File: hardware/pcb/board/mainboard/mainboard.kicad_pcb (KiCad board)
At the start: 6 copper layers, 76.4 x 55 mm, 137 parts, among them J1 Conn_Coaxial, J10 USB_C_Receptacle, J11 2908-05WB-MG, J2 USB_C_Receptacle_USB2.0_16P, J3 Conn_02x35_Odd_Even_MountingP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, J4 Conn_02x40_Odd_Even_MountingP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, J5 Conn_02x40_Odd_Even_MountingP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, J7 Conn_01x30, J8 Conn_01x30, J9 Conn_01x30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

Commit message: USB PD power
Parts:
- moved R18 33.9 mm to (169.0, 147.7), turned to 0 degrees
- moved R19 32.3 mm to (169.0, 146.1), turned to 0 degrees
- moved U14 24.1 mm to (168.2, 151.9), turned to 90 degrees
- moved C27 20.8 mm to (169.0, 149.3), turned to 0 degrees
- moved C26 18.5 mm to (162.1, 146.1)
- moved R22 16.1 mm to (149.8, 134.3)
- moved C33 16.1 mm to (153.0, 134.3)
- moved C34 16.1 mm to (152.9, 135.9)
- moved U12 10.2 mm to (158.2, 138.0), turned to 180 degrees
- moved R24 9.94 mm to (166.2, 133.6)
- moved R26 9.94 mm to (166.2, 135.2)
- moved C28 7.85 mm to (162.0, 140.6), turned to 0 degrees
- moved R23 6.24 mm to (159.0, 146.1), turned to 0 degrees
- moved C32 4.93 mm to (164.3, 138.3), turned to -90 degrees
- moved Q2 4.80 mm to (161.4, 143.3), turned to 0 degrees
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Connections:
- J2 pad GND: (no net) -> GND
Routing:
- net H_UART_RXD_1: track 0.00 -> 25.4 mm
- net H_UART_TXD_1: track 0.00 -> 25.0 mm
- net USB1_D-: track 0.00 -> 12.4 mm, vias 0 -> 3
- net USB1_D+: track 0.00 -> 11.3 mm, vias 0 -> 2
- net +1V8: track 0.00 -> 8.29 mm, vias 0 -> 2
- net USB1_VBUS: track 0.00 -> 7.45 mm
- net Net-(J2-CC2): track 0.00 -> 6.18 mm, vias 0 -> 2
- net Net-(J2-CC1): track 0.00 -> 4.68 mm
- net VBUS: track 0.00 -> 2.81 mm
- net GND: track 0.00 -> 1.83 mm
- net USB_D-: track 0.00 -> 1.61 mm
- net USB_D+: track 0.00 -> 0.75 mm, vias 0 -> 1
- added copper zone on B.Cu, net GND
- added copper zone on F.Cu, net GND
- added copper zone on In1.Cu, net GND
- added copper zone on In4.Cu, net GND

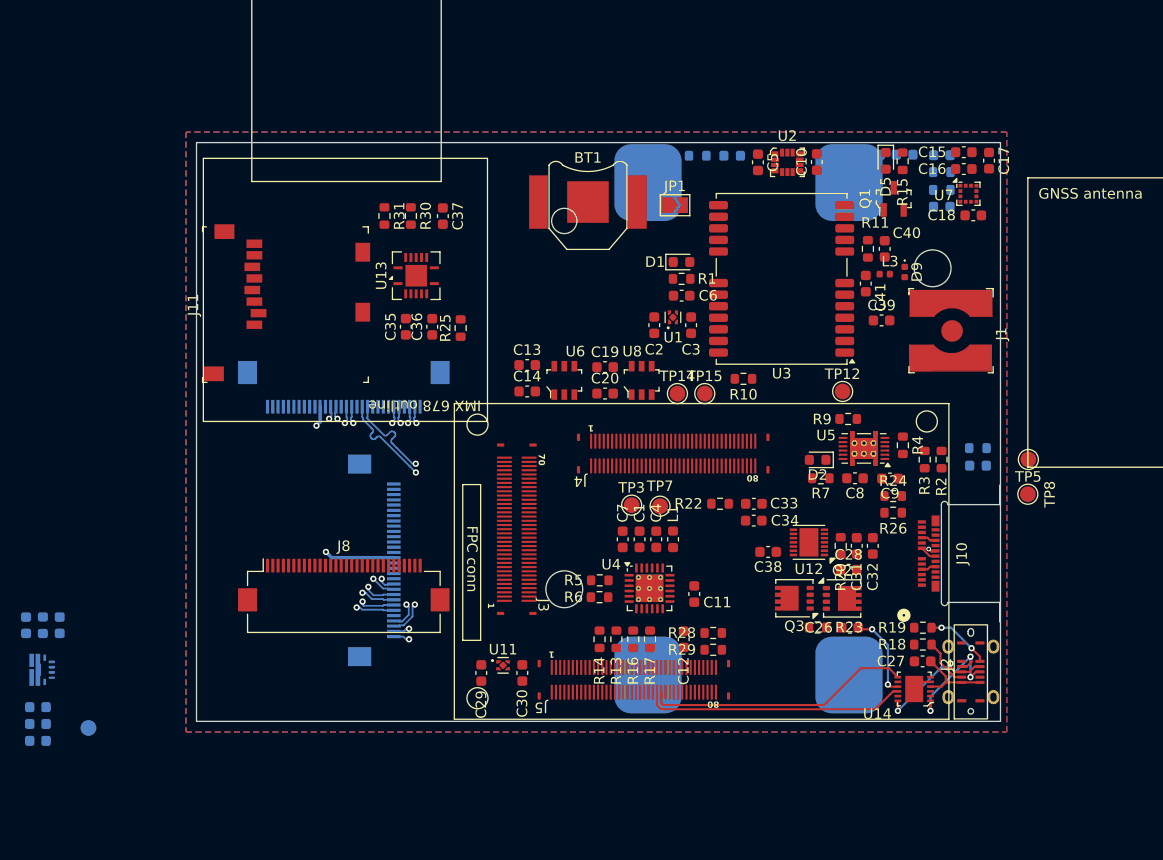
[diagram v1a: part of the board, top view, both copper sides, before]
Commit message: BQ25606 routing
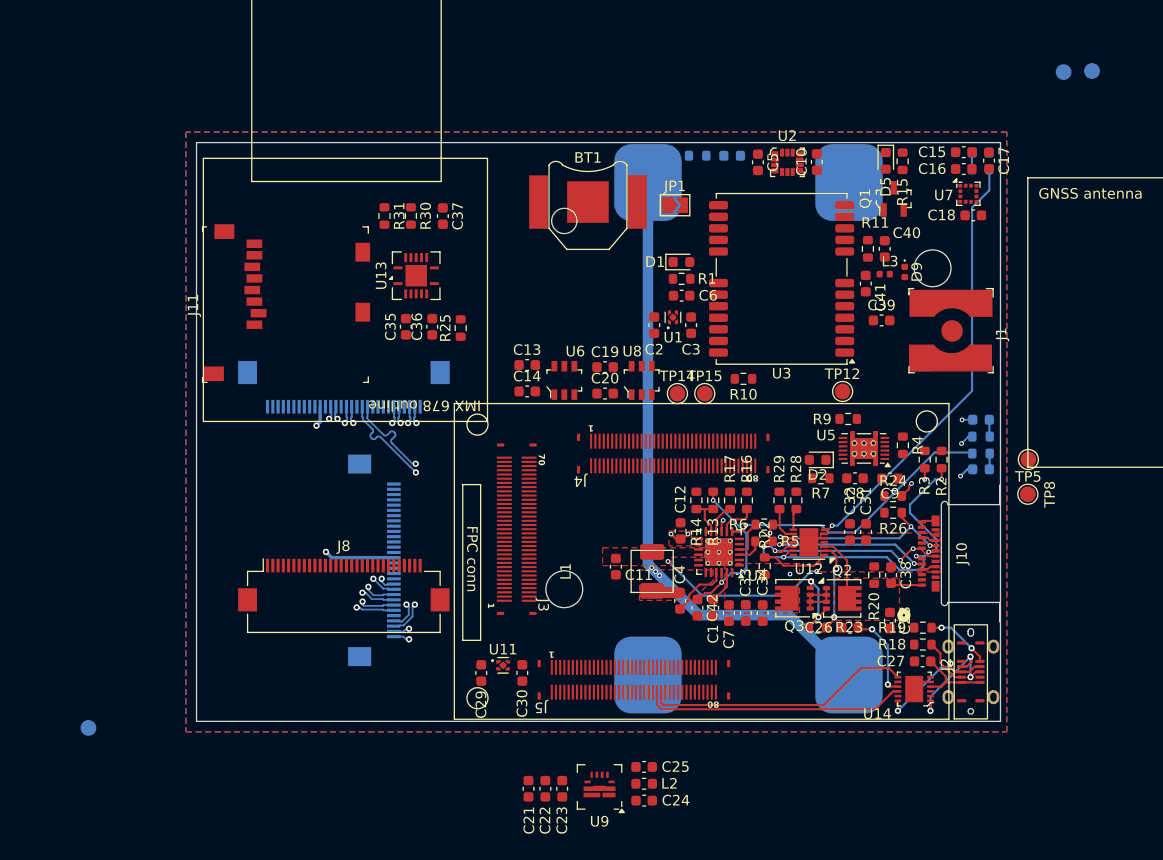
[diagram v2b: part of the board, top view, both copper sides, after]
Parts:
- removed D6: LED, LED_SMD:LED_0603_1608Metric
- removed R21: 100k, Resistor_SMD:R_0603_1608Metric
- added C42: 4.7 uF, Capacitor_SMD:C_0603_1608Metric, F.Cu at (147.6, 144.2)
- C21, C22, C23, C24, C25, L2, U9: moved to F.Cu
- L1: footprint Inductor_SMD:L_0603_1608Metric -> unsurv_offline_pcb_footprints:Inductor_Wuerth_74437321010
- TP3, TP7: moved to B.Cu
- moved C24 61.1 mm to (142.5, 162.5), turned to 180 degrees
- moved L2 59.1 mm to (142.5, 160.9), turned to 180 degrees
- moved TP7 58.3 mm to (185.1, 93.2)
- moved TP3 58.1 mm to (182.4, 93.3)
- moved C25 57.1 mm to (142.5, 159.3), turned to 180 degrees
- moved U9 54.4 mm to (138.3, 161.2), turned to 180 degrees
- moved C23 50.4 mm to (134.8, 161.4), turned to 90 degrees
- moved C22 48.6 mm to (133.2, 161.4), turned to 90 degrees
- moved C21 46.8 mm to (131.6, 161.4), turned to 90 degrees
- moved D4 30.8 mm to (174.6, 131.1)
- moved R12 30.2 mm to (174.6, 129.6)
- moved R32 23.7 mm to (174.6, 127.9)
- moved D8 20.6 mm to (174.6, 126.3), turned to 0 degrees
- moved R6 17.1 mm to (153.9, 136.3)
- moved R16 17.1 mm to (152.3, 134.0), turned to 90 degrees
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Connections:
- BT2 pad 2: B- -> GND
- J2 pad GND: GND -> (no net)
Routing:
- net B+: track 0.00 -> 61.7 mm, vias 0 -> 5
- net Net-(U12-LED): track 0.00 -> 41.2 mm, vias 0 -> 1
- net SYS: track 0.00 -> 35.3 mm, vias 0 -> 3
- net USB_D+: track 0.75 -> 33.6 mm, vias 1 -> 5
- net USB_D-: track 1.61 -> 30.3 mm, vias 0 -> 5
- net Net-(U4-PG): track 0.00 -> 26.7 mm, vias 0 -> 1
- net USB_CC1: track 0.00 -> 25.8 mm, vias 0 -> 3
- net USB_PD: track 0.00 -> 24.6 mm, vias 0 -> 2
- net USB_CC2: track 0.00 -> 19.0 mm, vias 0 -> 3
- net REGN: track 0.00 -> 15.4 mm, vias 0 -> 2
- net Net-(U12-PWR_EN): track 0.00 -> 8.51 mm, vias 0 -> 2
- net GND: track 1.83 -> 9.97 mm, vias 0 -> 2
- net Net-(Q2-G): track 0.00 -> 6.82 mm, vias 0 -> 2
- net Net-(U12-VOUT): track 0.00 -> 6.42 mm
- net Net-(Q2-D): track 0.00 -> 6.29 mm
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- added copper zone on F.Cu, net B+
- added copper zone on In3.Cu, net B+
- added copper zone on F.Cu, net Net-(C4-Pad2)
- added copper zone on F.Cu, net Net-(Q2-D)
- added copper zone on F.Cu, net SYS
- added copper zone on F.Cu, net USB_PD
- added copper zone on F.Cu, net VBUS

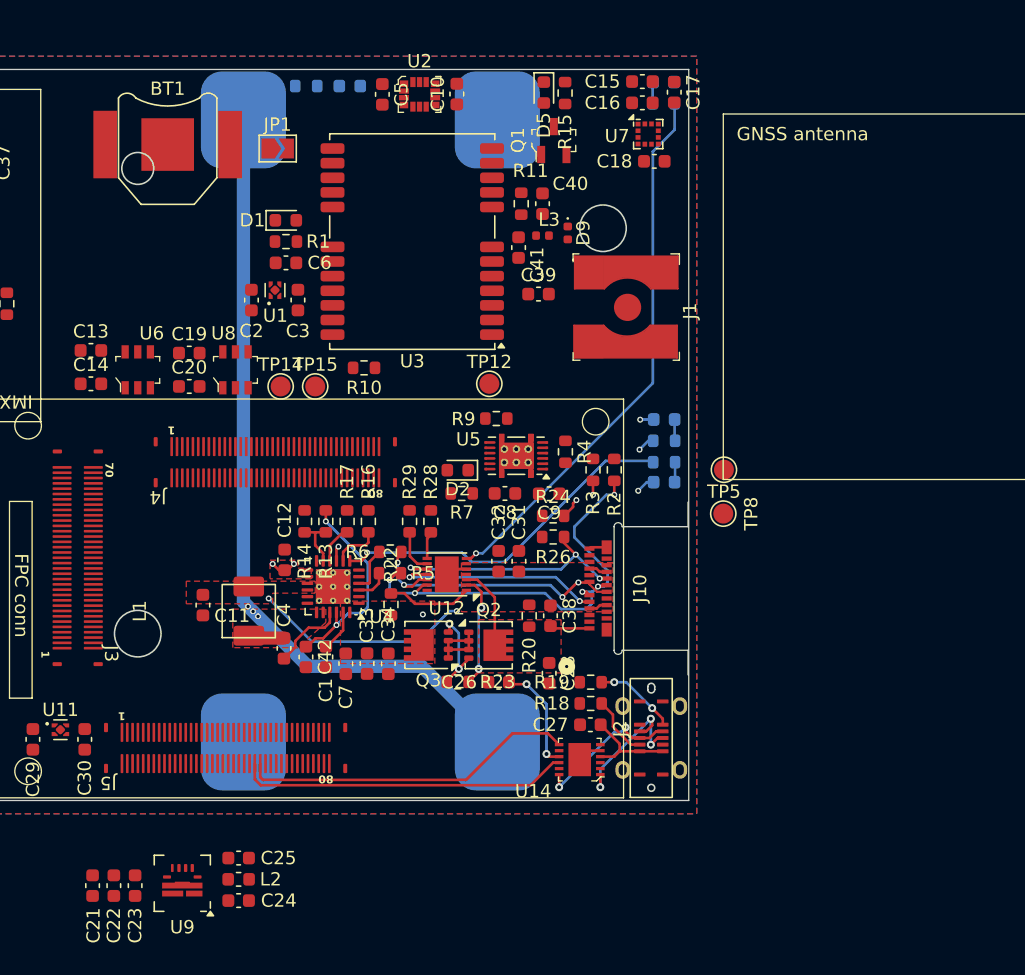
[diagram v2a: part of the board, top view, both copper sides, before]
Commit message: TPS61235p 5v PWR routing
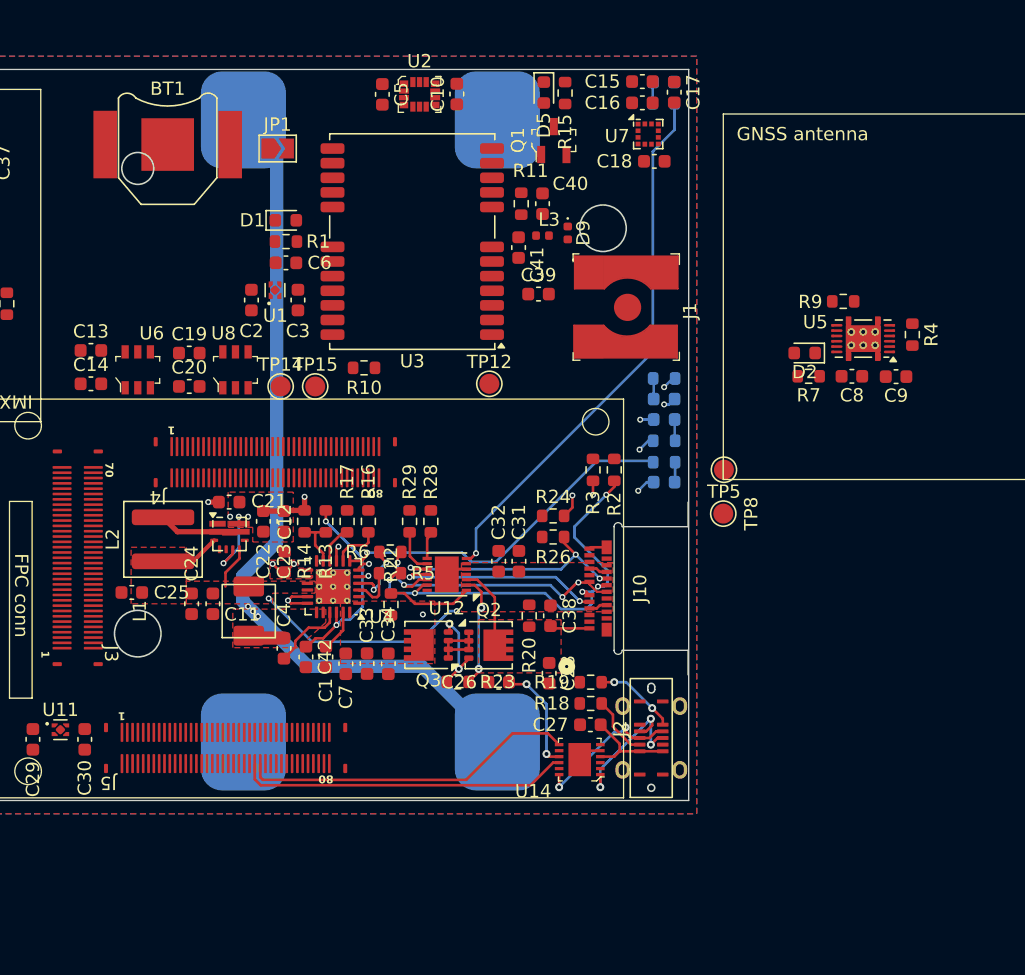
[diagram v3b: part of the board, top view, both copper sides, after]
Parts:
- L2: footprint Inductor_SMD:L_0603_1608Metric -> Inductor_SMD:L_Coilcraft_XAL5020-XXX
- moved R8 34.8 mm to (174.6, 123.2), turned to 0 degrees
- moved D3 33.4 mm to (174.6, 124.8)
- moved C21 30.6 mm to (141.8, 132.6), turned to 180 degrees
- moved C22 29.6 mm to (144.4, 134.0)
- moved C23 29.6 mm to (145.9, 134.0)
- moved C8 27.5 mm to (188.7, 123.1)
- moved R7 27.5 mm to (185.4, 123.1)
- moved C9 27.5 mm to (192.0, 123.1)
- moved D2 27.5 mm to (185.1, 121.3)
- moved R9 27.5 mm to (188.0, 117.5)
- moved U5 27.5 mm to (189.5, 120.2)
- moved R4 27.5 mm to (193.2, 120.0)
- moved U9 26.5 mm to (141.8, 134.9), turned to 0 degrees
- moved L2 26.2 mm to (136.8, 135.3), turned to 90 degrees
- moved C24 22.6 mm to (139.0, 140.2), turned to -90 degrees
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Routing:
- net Net-(U4-STAT): track 0.00 -> 34.5 mm, vias 0 -> 2
- net SYS: track 35.3 -> 51.3 mm, vias 3 -> 4
- net GND: track 9.97 -> 19.1 mm, vias 2 -> 6
- net +5V: track 0.00 -> 5.86 mm, vias 0 -> 4
- net Net-(U9-SW): track 0.00 -> 5.45 mm
- net B+: track 61.7 -> 64.0 mm
- net Net-(D3-K): track 0.00 -> 1.57 mm
- net Net-(U4-D-): track 3.44 -> 4.98 mm, vias 0 -> 2
- net Net-(U4-D+): track 2.47 -> 3.45 mm
- net REGN: track 15.4 -> 14.8 mm
- added copper zone on F.Cu, net +5V
- added copper zone on In3.Cu, net +5V

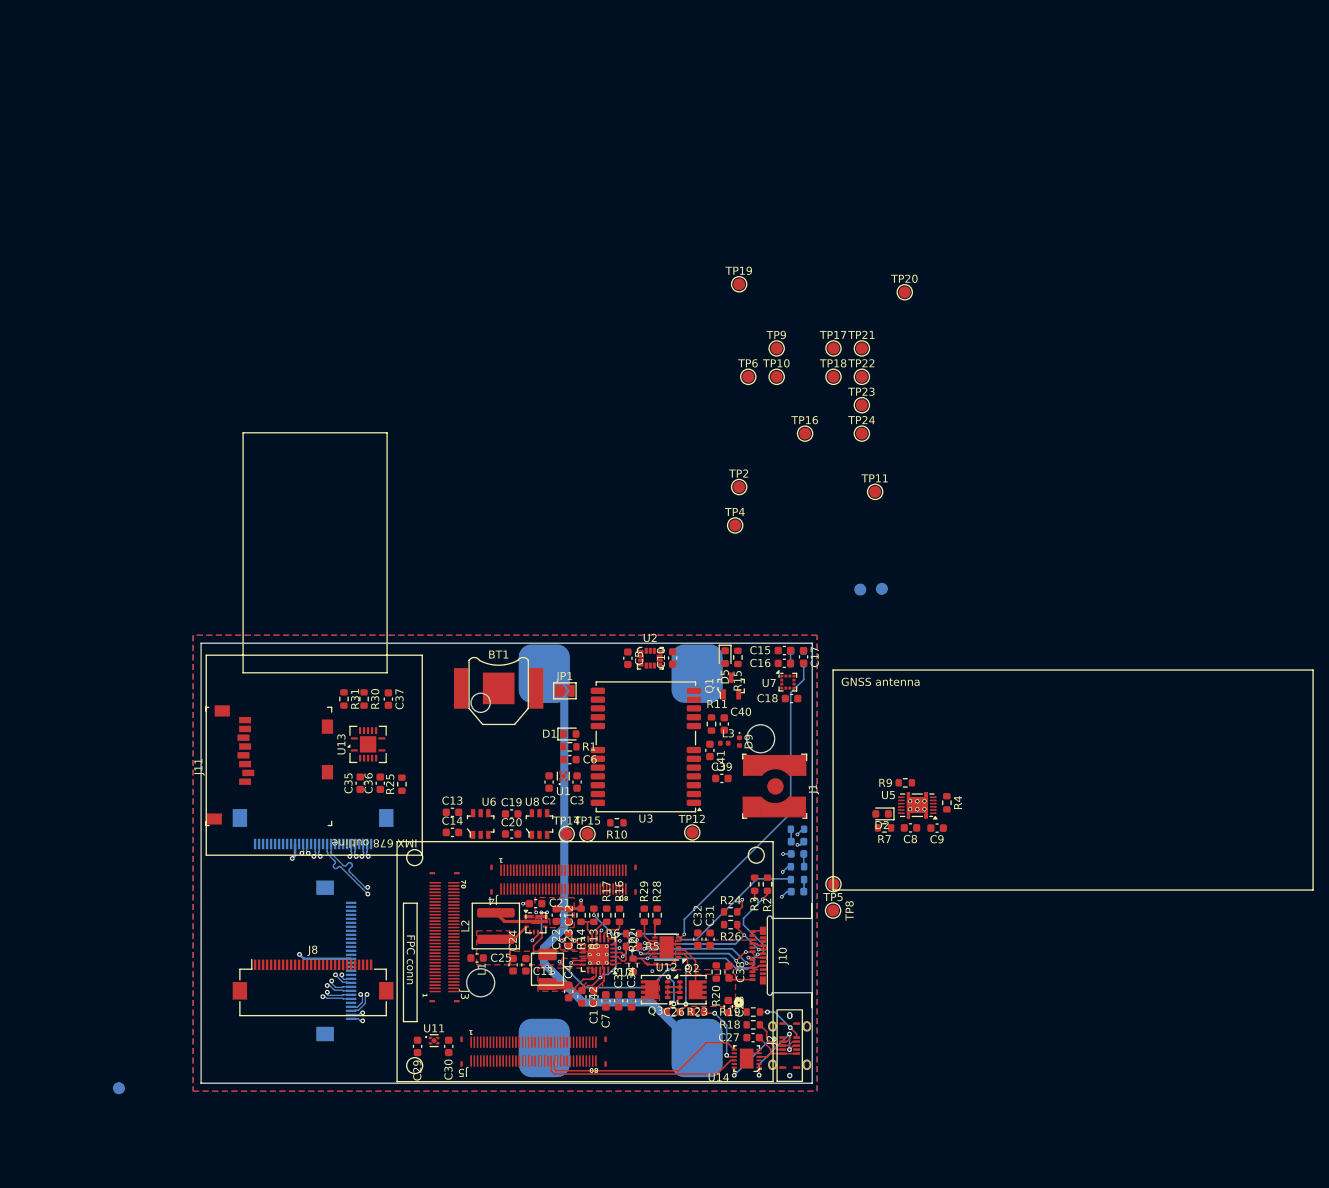
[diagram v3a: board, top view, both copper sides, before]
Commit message: route ublox GNSS receiver
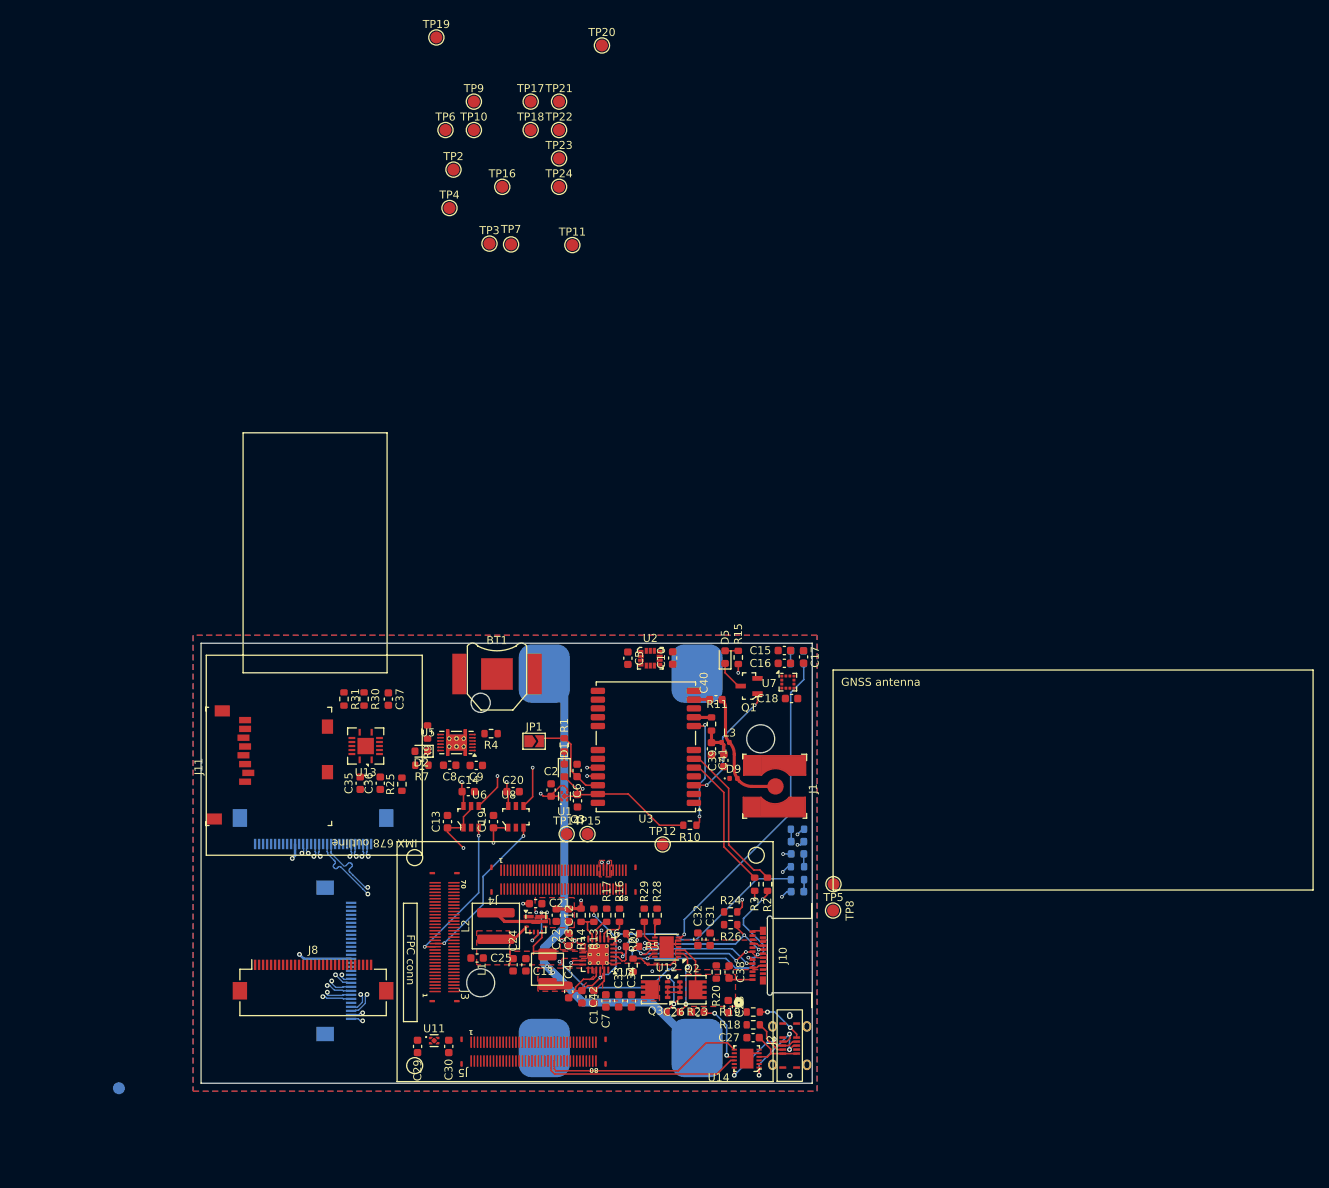
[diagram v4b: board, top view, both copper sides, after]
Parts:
- TP3, TP7: moved to F.Cu
- moved TP3 63.4 mm to (136.1, 50.0)
- moved TP7 63.3 mm to (138.8, 50.1)
- moved R9 60.1 mm to (128.3, 111.1), turned to -90 degrees
- moved R7 58.4 mm to (127.6, 115.2)
- moved C8 58.1 mm to (131.1, 115.2)
- moved C9 58.1 mm to (134.4, 115.3)
- moved D2 58.1 mm to (127.5, 113.5)
- moved U5 58.1 mm to (131.9, 112.4)
- moved R4 57.6 mm to (136.2, 111.3), turned to 180 degrees
- moved TP2 53.4 mm to (131.6, 40.8)
- moved TP4 53.4 mm to (131.1, 45.6)
- moved TP17 48.8 mm to (141.2, 32.3)
- moved TP18 48.8 mm to (141.2, 35.9)
- moved TP10 48.8 mm to (134.1, 35.9)
- moved TP11 48.8 mm to (146.4, 50.2)
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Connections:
- R10 pad 1: +3V3 -> GNSS_3V3
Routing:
- net GNSS_3V3: track 0.00 -> 76.4 mm, vias 0 -> 4
- net H_UART_RXD_2: track 0.00 -> 19.7 mm, vias 0 -> 2
- net Net-(U3-USB_DP): track 0.00 -> 19.5 mm
- net H_UART_TXD_2: track 0.00 -> 19.0 mm, vias 0 -> 2
- net UBLOX_RX_3V3: track 0.00 -> 17.3 mm, vias 0 -> 2
- net Net-(U3-USB_DM): track 0.00 -> 17.3 mm
- net PPS: track 0.00 -> 15.7 mm, vias 0 -> 2
- net Net-(J1-In): track 0.00 -> 15.4 mm
- net Net-(U3-~{RESET}): track 0.00 -> 14.5 mm, vias 0 -> 2
- net VDD_1V8: track 0.00 -> 14.4 mm, vias 0 -> 4
- net UBLOX_TX_3V3: track 0.00 -> 13.4 mm, vias 0 -> 2
- net V_BCKP: track 0.00 -> 11.8 mm
- net +5V: track 5.86 -> 12.0 mm, vias 4 -> 5
- net Net-(C39-Pad2): track 0.00 -> 4.37 mm
- net Net-(D5-K): track 0.00 -> 3.81 mm
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- added copper zone on F.Cu, net VDD_1V8
- added copper zone on In3.Cu, net VDD_1V8
